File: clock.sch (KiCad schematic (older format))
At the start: 16 parts, among them P4 Clock, U2 4011, U6 4011, U7 LM555N

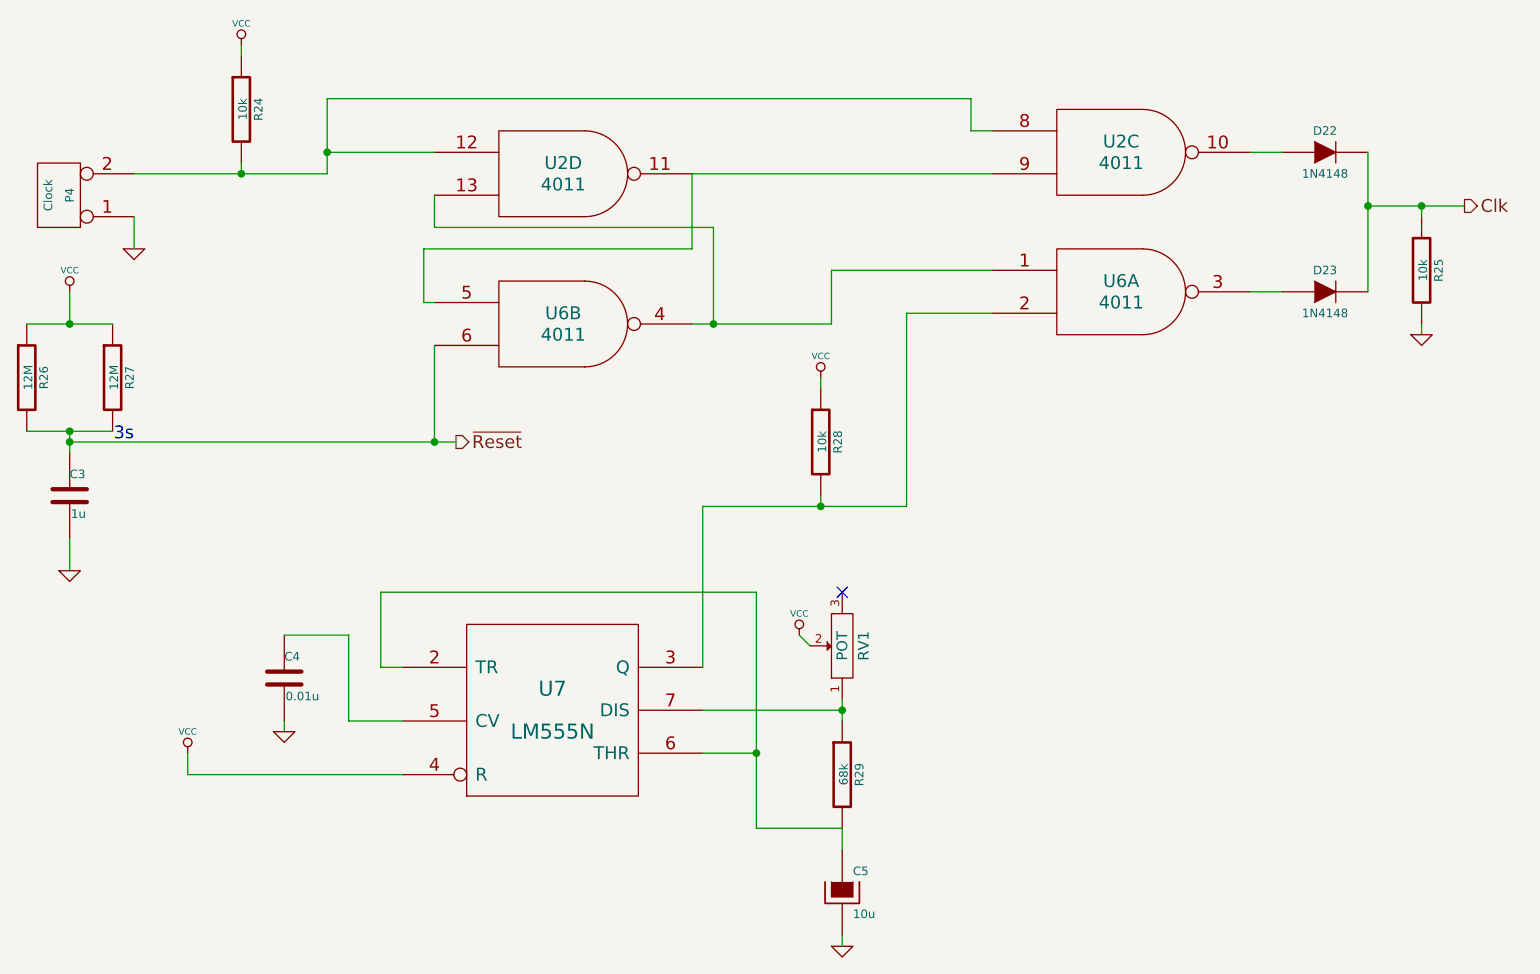
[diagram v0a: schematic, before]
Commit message: Removed external clock circuit.
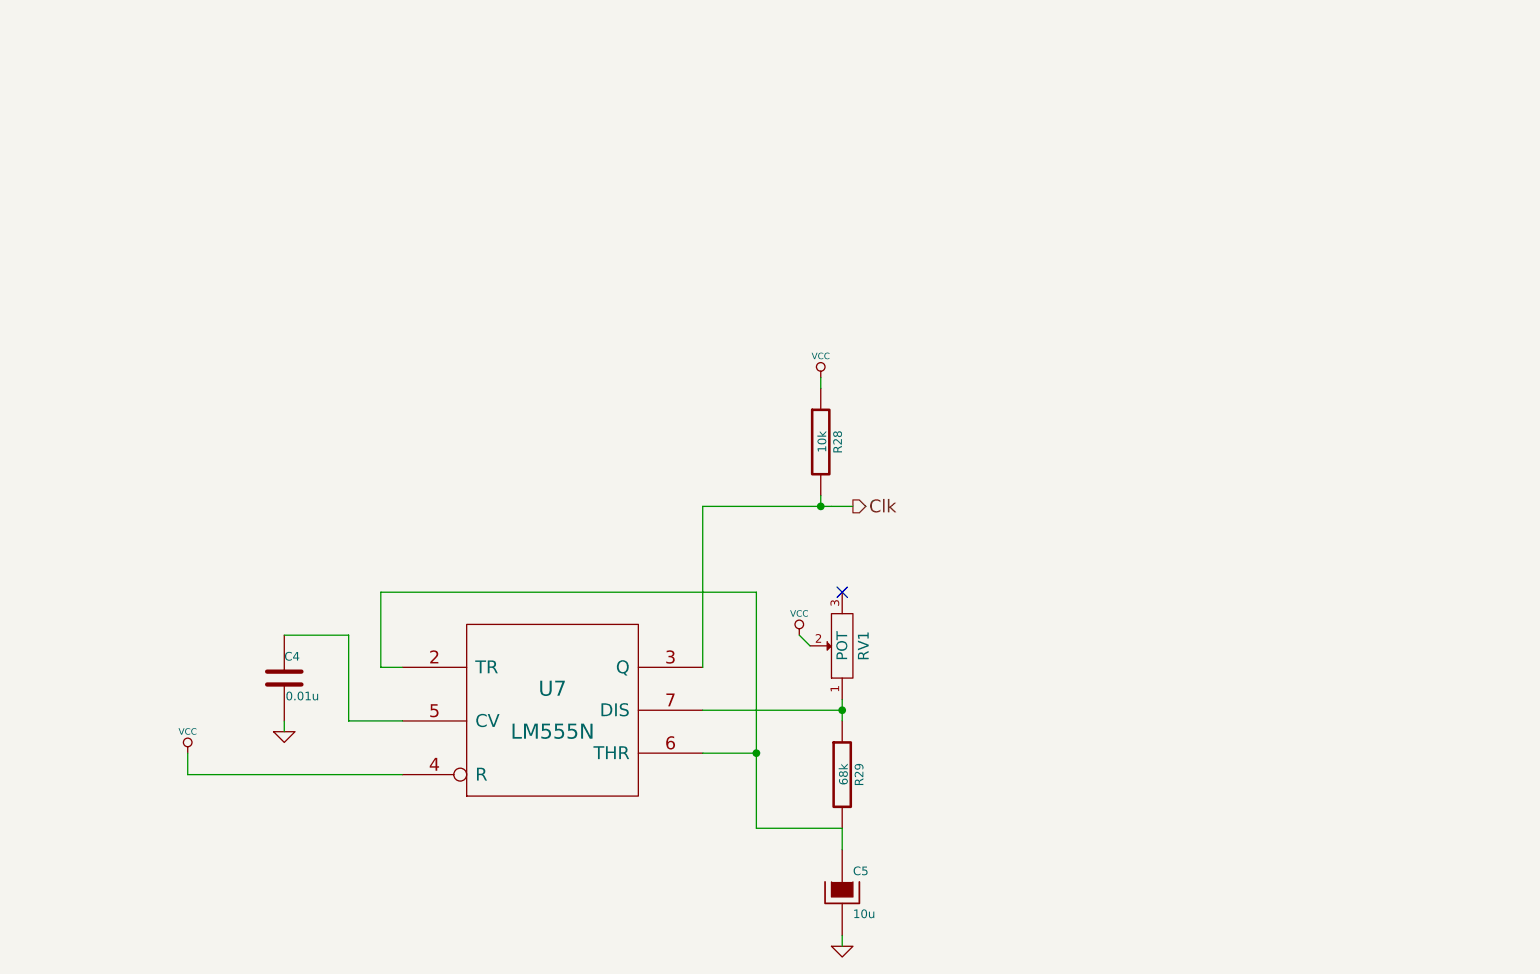
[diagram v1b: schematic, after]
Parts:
- removed C3: 1u, ~, symbol C
- removed D22, D23: 1N4148, ~, symbol DIODE
- removed P4: Clock, symbol CONN_2
- removed R24, R25: 10k, ~, symbol R
- removed R26, R27: 12M, ~, symbol R
- removed U2, U6: 4011, symbol 4011
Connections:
- net Clk: now also R28.2, U7.3 (Q)
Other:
- note removed: "3s"
